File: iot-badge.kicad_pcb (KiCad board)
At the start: 2 copper layers, 70 x 100 mm, 46 parts, among them J1 USB_C_Receptacle_USB2.0, J2 Conn_01x01_Male, Q1 BC847, Q2 BC847, SW1 SW_Push, SW2 SW_Push, SW3 SW_Push, SW4 SW_Push, SW5 SW_Push, SW6 SW_Push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

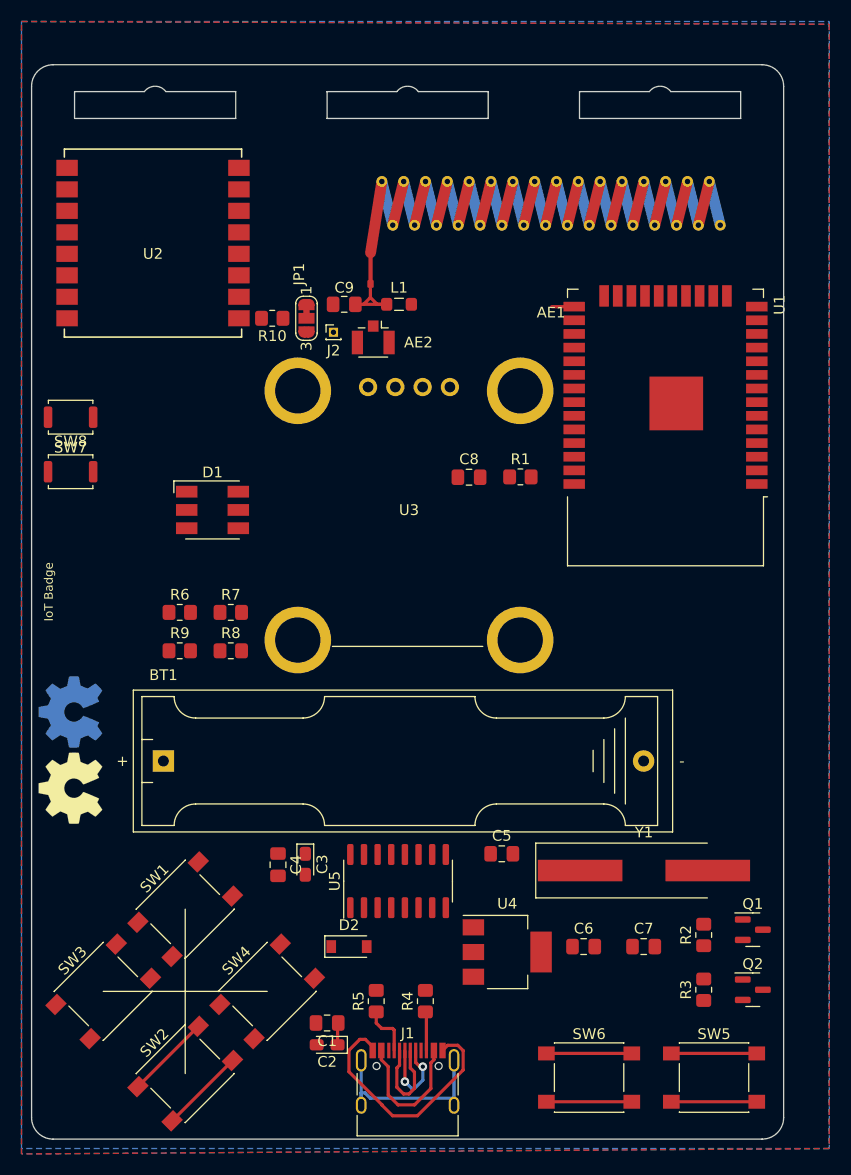
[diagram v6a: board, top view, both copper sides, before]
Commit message: power switch added
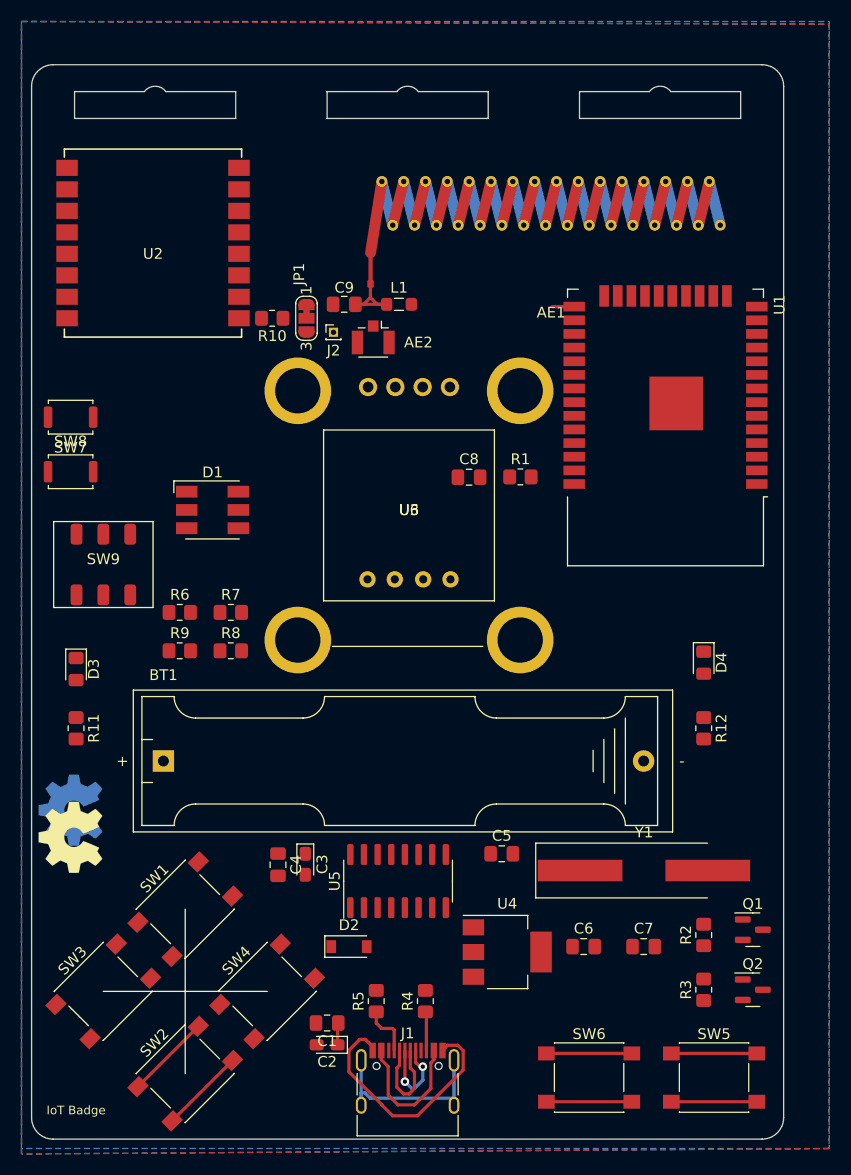
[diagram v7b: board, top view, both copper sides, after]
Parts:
- added D3: BATLED, LED_SMD:LED_0805_2012Metric_Pad1.15x1.40mm_HandSolder, F.Cu at (104.1, 106.2)
- added D4: USBLED, LED_SMD:LED_0805_2012Metric_Pad1.15x1.40mm_HandSolder, F.Cu at (162.6, 105.7)
- added R11: 1k, Resistor_SMD:R_0805_2012Metric_Pad1.20x1.40mm_HandSolder, F.Cu at (104.1, 111.8)
- added R12: 1k, Resistor_SMD:R_0805_2012Metric_Pad1.20x1.40mm_HandSolder, F.Cu at (162.6, 111.8)
- added SW9: SW_PWR_USB_BAT, Slide_Switch_SMD:SW_Slide_2P2T_9mmx7.6mm, F.Cu at (106.7, 96.5)
- added U6: ME2188_PCB_MODULE, DCDC_mini_PCB_module:ME2188_PCB_MODULE, F.Cu at (135.1, 91.9)
- J2: value Conn_01x01_Male -> Wire ANT
- R10: value R -> 0
- moved SYMB1 9.14 mm to (103.6, 119.4)
- moved SYMB2 4.57 mm to (103.6, 121.9)
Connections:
- BT1 pad 1: unconnected-(BT1-Pad1) -> +BATT
- BT1 pad 2: unconnected-(BT1-Pad2) -> Earth
- C3 pad 1: +3V3 -> +3.3VP
- C4 pad 1: +3V3 -> +3.3VP
- C5 pad 1: +3V3 -> +3.3VP
- U4 pad 2: +3V3 -> +3.3VP
- U5 pad 16: +3V3 -> +3.3VP
- U5 pad 4: +3V3 -> +3.3VP

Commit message: added ground to pushbuttons
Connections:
- SW3 pad 2: unconnected-(SW3-Pad2) -> Earth
- SW4 pad 2: unconnected-(SW4-Pad2) -> Earth
- SW5 pad 2: unconnected-(SW5-Pad2) -> Earth
- SW6 pad 2: unconnected-(SW6-Pad2) -> Earth
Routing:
- net Earth: track 23.5 -> 39.4 mm
- net unconnected-(SW6-Pad2): track 7.95 -> 0.00 mm
- net unconnected-(SW5-Pad2): track 7.95 -> 0.00 mm
